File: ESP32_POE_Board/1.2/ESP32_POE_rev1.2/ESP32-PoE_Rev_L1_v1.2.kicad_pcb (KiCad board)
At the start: 4 copper layers, 81.5 x 92.3 mm, 133 parts, among them Q1 Q12MHz/20pF/10ppm/4P/3.2x2.5mm, Q2 BC817-40(SOT23), Q3 BC817-40(SOT23), T1 LMUN2211LT1G(SOT-23), U1 CH340T(SSOP20W), U2 TPS2375D(SO-8), U3 BL4054B-42TPRN(SOT23-5), U4 LAN8710A-EZC(QFN32), U5 TX4138(ESOIC-8), U6 ESP32-WROVER-E, U7 SY8089AAAC(SOT23-5), U8 SN74LVC1G04DBVR(SOT23-5)

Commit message: fixing POE board symbols + circuit
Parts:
- removed BAT_SENS_E1: Opened, OLIMEX_Jumpers-FP:SJ_1_SMALLER
- removed C22: 47uF/6.3V/20%/X5R/C0805, OLIMEX_RLC-FP:C_0805_5MIL_DWS
- removed CHRG1: LED/YELLOW/0603, OLIMEX_LEDs-FP:LED_0603_KA
- removed EXT1, EXT2: NS(HN1x10), OLIMEX_Connectors-FP:HN1x10
- removed FET1, FET2: WPM2015-3/TR, OLIMEX_Transistors-FP:SOT23
- removed L2: 2.2uH/1.5A/DCR=72mR/20%/3.00x3.00x1.50mm/CD32(NR3015T2R2M), OLIMEX_RLC-FP:CD32
- removed L5: FB0805/600R/2A, OLIMEX_RLC-FP:L_0805_5MIL_DWS
- removed PWR1: LED/RED/0603, OLIMEX_LEDs-FP:LED_0603_KA
- removed R17, R22: 470k/R0402, OLIMEX_RLC-FP:R_0402_5MIL_DWS
- removed R29: 220k/R0402, OLIMEX_RLC-FP:R_0402_5MIL_DWS
- removed R30: 49.9k/1%/R0402, OLIMEX_RLC-FP:R_0402_5MIL_DWS
- removed R39, R6: 10k/R0402, OLIMEX_RLC-FP:R_0402_5MIL_DWS
- removed R40, R45: 10R/R0402, OLIMEX_RLC-FP:R_0402_5MIL_DWS
- removed R46: 220R/R0402, OLIMEX_RLC-FP:R_0402_5MIL_DWS
- removed R8: 2.2k/R0402, OLIMEX_RLC-FP:R_0402_5MIL_DWS
- removed R9: 100k/R0402, OLIMEX_RLC-FP:R_0402_5MIL_DWS
- removed RM3: RA1206_(4X0603)_4B8_2.2k, OLIMEX_RLC-FP:R_MATRIX_4
- added C29: 1uF, Capacitor_SMD:C_0201_0603Metric, F.Cu at (159.8, 125.9)
- added C30: 10uF, Capacitor_SMD:C_0603_1608Metric, F.Cu at (156.0, 141.0)
- added C31: 1uF, Capacitor_SMD:C_0201_0603Metric, F.Cu at (159.8, 127.6)
- added D10: BAT54C, Package_TO_SOT_SMD:SOT-23, F.Cu at (147.1, 131.5)
- added D11: 1N5819, Diode_THT:D_DO-41_SOD81_P10.16mm_Horizontal, F.Cu at (146.5, 127.1)
- added FB1: 600R-2A, Capacitor_SMD:C_0805_2012Metric, F.Cu at (151.8, 141.3)
- added J1: USB_C_Receptacle, Connector_USB:USB_C_Receptacle_Molex_105450-0101-L, F.Cu at (155.7, 134.2)
- added J2: SI-46020-F, SI-46020-F:BEL_SI-46020-F, F.Cu at (153.1, 156.2)
- added Q4: BC817, Package_TO_SOT_SMD:SOT-23, F.Cu at (147.1, 135.9)
- added Q5: BC817, Package_TO_SOT_SMD:SOT-23, F.Cu at (147.1, 140.4)
- added U9: LAN8710A-EZC, LAN8710A_EZC:QFN32_5X5MC_MCH, F.Cu at (146.5, 167.6)
- C1: value 22uF/6.3V/20%/X5R/C0603 -> 10uF; footprint OLIMEX_RLC-FP:C_0603_5MIL_DWS -> Capacitor_SMD:C_0603_1608Metric
- C19: value 1nF/50V/10%/X7R/C0402 -> 1nF; footprint OLIMEX_RLC-FP:C_0402_5MIL_DWS -> Capacitor_SMD:C_1206_3216Metric; moved to F.Cu
- C28: value 100nF/16V/10%/X7R/C0402 -> 10uF; footprint OLIMEX_RLC-FP:C_0402_5MIL_DWS -> Capacitor_SMD:C_0603_1608Metric
- C3: value 47uF/6.3V/20%/X5R/C0805 -> 100nF; footprint OLIMEX_RLC-FP:C_0805_5MIL_DWS -> Capacitor_SMD:C_0402_1005Metric; moved to F.Cu
- C6: value 22uF/6.3V/20%/X5R/C0603 -> 1uF; footprint OLIMEX_RLC-FP:C_0603_5MIL_DWS -> Capacitor_SMD:C_0201_0603Metric
- D1, D3: value 1N5822/SS34/SMA -> 1N5819; footprint OLIMEX_Diodes-FP:SMA-KA -> Diode_THT:D_DO-41_SOD81_P10.16mm_Horizontal
- R1: value 10k/R0402 -> 1k; footprint OLIMEX_RLC-FP:R_0402_5MIL_DWS -> Resistor_SMD:R_0402_1005Metric
- R4: value 47k/R0402 -> 1k; footprint OLIMEX_RLC-FP:R_0402_5MIL_DWS -> Resistor_SMD:R_0402_1005Metric
- R5: value 2.2k/R0402 -> 220; footprint OLIMEX_RLC-FP:R_0402_5MIL_DWS -> Resistor_SMD:R_0402_1005Metric
- U3: value BL4054B-42TPRN(SOT23-5) -> FT232RQ; footprint OLIMEX_IC-FP:SOT-23-5 -> FT232RQ:QFN50P500X500X90-33N
- U7: value SY8089AAAC(SOT23-5) -> ESDS314DBVR; footprint OLIMEX_Regulators-FP:SOT-23-5 -> ESDS314DBVR:DBV0005A_N
- U8: value SN74LVC1G04DBVR(SOT23-5) -> MIC5504-3.3YM5; footprint OLIMEX_IC-FP:SOT-23-5 -> Package_TO_SOT_SMD:SOT-23-5
- moved C3 79.5 mm to (157.4, 169.4), turned to 0 degrees
- moved C19 62.0 mm to (153.1, 165.4)
- moved U7 58.3 mm to (158.6, 166.1), turned to 0 degrees
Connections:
- net /ESP_EN renamed ESP_EN
- net /GPIO2\HS2_DATA0 renamed GPIO2\HS2_DATA0
- C19 pad 1: Net-(BAT_SENS_E1-Pad2) -> GND
- C19 pad 2: GND -> Net-(C19-Pad2)
- C28 pad 1: GND -> +5VP
- C28 pad 2: +3.3VLAN -> GND
- C3 pad 1: Net-(MICRO_SD1-VDD) -> unconnected-(C3-Pad1)
- C3 pad 2: GND -> unconnected-(C3-Pad2)
- C6 pad 1: Net-(D3-K) -> +5V
- D1 pad 1: +5V -> Net-(D1-K)
- D1 pad 2: +5VP -> GPIO3_U0RXD
- D2 pad 2: /GPIO0 -> GPIO0
- D3 pad 1: Net-(D3-K) -> GPIO1_U0TXD
- D3 pad 2: +5V -> Net-(D3-A)
- R1 pad 1: +5V -> Net-(Q5-C)
- R1 pad 2: GND -> Net-(Q4-B)
- R4 pad 1: +5V -> Net-(Q4-E)
- R4 pad 2: /GPI39 -> Net-(Q5-B)
- R44 pad 1: /GPIO0 -> GPIO0
- R5 pad 2: GND -> Net-(D10-Pad3)
- U3 pad 1: Net-(U3-CHRGb) -> +5V
- U3 pad 2: GND -> Net-(D3-A)
- U3 pad 3: Net-(U3-VBAT) -> unconnected-(U3-~{RI}-Pad3)
- U3 pad 4: +5V -> Net-(U3-GND-Pad17)
- U3 pad 5: Net-(U3-PROG) -> (no net)
- U6 pad 25: /GPIO0 -> GPIO0
- U7 pad 1: Net-(D3-K) -> unconnected-(U7-I_O1-Pad1)
- U7 pad 2: GND -> unconnected-(U7-GND-Pad2)
- U7 pad 3: Net-(U7-LX) -> unconnected-(U7-I_O2-Pad3)
- U7 pad 4: Net-(D3-K) -> unconnected-(U7-I_O3-Pad4)
- U7 pad 5: Net-(U7-FB) -> unconnected-(U7-I_O4-Pad5)
- U8 pad 1: unconnected-(U8-NC-Pad1) -> +5VP
- U8 pad 2: /GPIO0 -> GND
- U8 pad 3: GND -> +5VP
- U8 pad 4: /GPIO17\EMAC_CLK_OUT_180 -> unconnected-(U8-NC-Pad4)
- U8 pad 5: +3.3VLAN -> +3.3V
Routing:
- net /GPIO0: track 67.8 -> 0.00 mm, vias 2 -> 0
- net /GPIO32: track 60.9 -> 0.00 mm, vias 2 -> 0
- net Net-(Q5-B): track 0.00 -> 60.8 mm, vias 0 -> 3
- net /GPI39: track 60.8 -> 0.00 mm, vias 3 -> 0
- net GND: track 380.7 -> 440.0 mm
- net GPIO0: track 0.00 -> 57.2 mm, vias 0 -> 2
- net (no net): track 0.00 -> 52.2 mm, vias 0 -> 3
- net Net-(D3-K): track 17.9 -> 0.00 mm
- net Net-(U7-FB): track 7.79 -> 0.00 mm, vias 2 -> 0
- net Net-(U3-CHRGb): track 5.24 -> 0.00 mm, vias 1 -> 0
- net Net-(U7-LX): track 4.89 -> 0.00 mm
- net Net-(BAT_SENS_E1-Pad2): track 2.97 -> 0.00 mm
- net +5V: track 91.6 -> 89.3 mm
- net Net-(Q5-C): track 0.00 -> 2.27 mm
- net Net-(U3-PROG): track 1.55 -> 0.00 mm
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
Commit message: updates
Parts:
- added SW1: PTS815 SJM 250 SMTR LFS, PTS815:SW4_PTS815 SJM 250 SMTR LFS_CNK, F.Cu at (179.0, 149.9)
- added SW2: PTS815 SJM 250 SMTR LFS, PTS815:SW4_PTS815 SJM 250 SMTR LFS_CNK, F.Cu at (179.0, 156.6)
- added U10: ESP32-WROOM-32, RF_Module:ESP32-WROOM-32, F.Cu at (198.3, 134.8)
- added U11: TPS2375D, LM193DR:D8, F.Cu at (186.8, 149.2)
- added U12: LM5145RGYR, LM5145RGYR:RGY0020B, F.Cu at (185.1, 155.5)

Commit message: fixing ethernet and poe power circuits
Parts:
- added C22: 22uF, Capacitor_SMD:C_0603_1608Metric, F.Cu at (215.6, 148.8)
- added C32: 100nF, Capacitor_SMD:C_0402_1005Metric, F.Cu at (223.1, 143.9)
- added C33: 2.2uF, Capacitor_SMD:C_0402_1005Metric, F.Cu at (223.1, 145.9)
- added C34: 100nF, Capacitor_SMD:C_0402_1005Metric, F.Cu at (223.1, 147.9)
- added C35: 100nF, Capacitor_SMD:C_0402_1005Metric, F.Cu at (223.1, 149.9)
- added D12: LED, LED_SMD:LED_0603_1608Metric, F.Cu at (224.3, 138.3)
- added D13: LED, LED_SMD:LED_0603_1608Metric, F.Cu at (224.3, 140.9)
- added D14: SMAJ58A, Diode_SMD:D_SMA, F.Cu at (217.6, 145.2)
- added R17: 2.2k, Resistor_SMD:R_0402_1005Metric, F.Cu at (217.9, 138.0)
- added R22: 130k, Resistor_SMD:R_0402_1005Metric, F.Cu at (217.9, 140.0)
- added R29: 10k, Resistor_SMD:R_0402_1005Metric, F.Cu at (217.9, 142.0)
- added R30: 10k, Resistor_SMD:R_0402_1005Metric, F.Cu at (220.8, 138.0)
- added R39: 4.42k, Resistor_SMD:R_0402_1005Metric, F.Cu at (220.8, 140.0)
- added R40: 24.9k, Resistor_SMD:R_0402_1005Metric, F.Cu at (220.8, 142.0)
- added R6: 2.2k, Resistor_SMD:R_0402_1005Metric, F.Cu at (215.0, 138.0)
- added R8: 2.2k, Resistor_SMD:R_0402_1005Metric, F.Cu at (215.0, 140.0)
- added R9: 2.2k, Resistor_SMD:R_0402_1005Metric, F.Cu at (215.0, 142.0)
- U12: value LM5145RGYR -> TX4138; footprint LM5145RGYR:RGY0020B -> TX4138:ESOIC8_XDS
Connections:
- C1 pad 1: +5V -> RCT
- C3 pad 1: unconnected-(C3-Pad1) -> GND
- C3 pad 2: unconnected-(C3-Pad2) -> RCT
- C6 pad 1: +5V -> RCT
- FB1 pad 1: +5V -> RCT
- J1 pad A1: +5V -> RCT
- J1 pad A12: +5V -> RCT
- J1 pad A4: +5V -> RCT
- J1 pad A9: +5V -> RCT
- J1 pad B1: +5V -> RCT
- J1 pad B12: +5V -> RCT
- J1 pad B4: +5V -> RCT
- J1 pad B9: +5V -> RCT
- J1 pad S1: +5V -> RCT
- J2 pad 1: unconnected-(J2-TD+-Pad1) -> TD+
- J2 pad 2: unconnected-(J2-TCT-Pad2) -> RCT
- J2 pad 3: unconnected-(J2-TD--Pad3) -> TD-
- J2 pad 4: unconnected-(J2-RD+-Pad4) -> RD+
- J2 pad 5: unconnected-(J2-RCT-Pad5) -> RCT
- J2 pad 6: unconnected-(J2-RD--Pad6) -> RD-
- LAN_CON1 pad 1: /TD+ -> TD+
- LAN_CON1 pad 2: /TD- -> TD-
- LAN_CON1 pad 3: /RD+ -> RD+
- LAN_CON1 pad 6: /RD- -> RD-
- R10 pad 2: /RD- -> RD-
- R11 pad 2: /RD+ -> RD+
- R12 pad 2: /TD- -> TD-
- R13 pad 2: /TD+ -> TD+
- TVS1 pad 1: /RD+ -> RD+
- TVS1 pad 3: /TD+ -> TD+
- TVS1 pad 4: /TD- -> TD-
- TVS1 pad 5: /RD- -> RD-
- TVS2 pad 1: /TD- -> TD-
- TVS2 pad 2: /TD+ -> TD+
- TVS3 pad 1: /RD+ -> RD+
- TVS3 pad 2: /RD- -> RD-
- U11 pad 1: unconnected-(U11-ILIM-Pad1) -> Net-(U11-ILIM)
- U11 pad 2: unconnected-(U11-CLASS-Pad2) -> Net-(U11-CLASS)
- U11 pad 3: unconnected-(U11-DET-Pad3) -> Net-(U11-DET)
- U11 pad 4: unconnected-(U11-VSS-Pad4) -> PW-
- U11 pad 5: unconnected-(U11-RTN-Pad5) -> GND
- U11 pad 7: unconnected-(U11-NC-Pad7) -> Net-(U11-NC)
- U3 pad 1: +5V -> RCT
- U3 pad 19: +5V -> RCT
- U4 pad 28: /TD- -> TD-
- U4 pad 29: /TD+ -> TD+
- U4 pad 30: /RD- -> RD-
- U4 pad 31: /RD+ -> RD+
- U7 pad 1: unconnected-(U7-I_O1-Pad1) -> TD+
- U7 pad 2: unconnected-(U7-GND-Pad2) -> GND
- U7 pad 3: unconnected-(U7-I_O2-Pad3) -> RD+
- U7 pad 4: unconnected-(U7-I_O3-Pad4) -> TD-
- U7 pad 5: unconnected-(U7-I_O4-Pad5) -> RD-
- U9 pad 1: unconnected-(U9-VDD2A-Pad1) -> RCT
- U9 pad 12: unconnected-(U9-VDDIO-Pad12) -> RCT
- U9 pad 15: unconnected-(U9-COL/CRS_DV/*MODE2-Pad15) -> GPIO27/EMAC_RX_CRS_DV
- U9 pad 16: unconnected-(U9-MDIO-Pad16) -> GPIO18/MDIO(RMII)
- U9 pad 2: unconnected-(U9-LED2/*NINTSEL-Pad2) -> Net-(D12-K)
- U9 pad 27: unconnected-(U9-VDD1A-Pad27) -> RCT
- U9 pad 3: unconnected-(U9-LED1/*REGOFF-Pad3) -> Net-(D13-A)
- U9 pad 5: unconnected-(U9-XTAL1/CLKIN-Pad5) -> GPIO17/EMAC_CLK_OUT_180
- U9 pad 6: unconnected-(U9-VDDCR-Pad6) -> RCT
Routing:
- net (no net): track 52.2 -> 141.6 mm
- net +5V: track 89.3 -> 0.00 mm, vias 4 -> 0
- net TD+: track 0.00 -> 25.5 mm, vias 0 -> 2
- net /TD+: track 25.5 -> 0.00 mm, vias 2 -> 0
- net /TD-: track 25.0 -> 0.00 mm, vias 2 -> 0
- net TD-: track 0.00 -> 24.9 mm, vias 0 -> 2
- net RD+: track 0.00 -> 13.3 mm, vias 0 -> 1
- net /RD+: track 13.3 -> 0.00 mm, vias 1 -> 0
- net RD-: track 0.00 -> 12.8 mm, vias 0 -> 1
- net /RD-: track 12.8 -> 0.00 mm, vias 1 -> 0
- net RCT: vias 0 -> 4

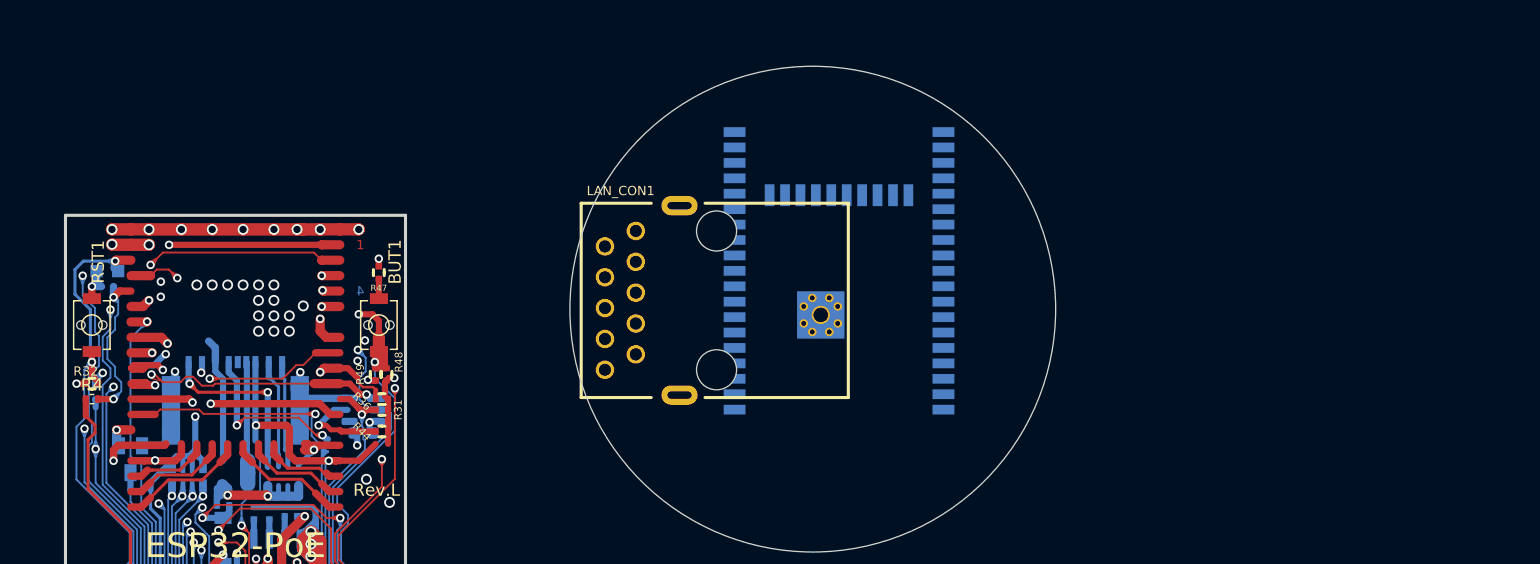
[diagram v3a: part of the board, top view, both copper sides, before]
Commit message: POE board partitioning
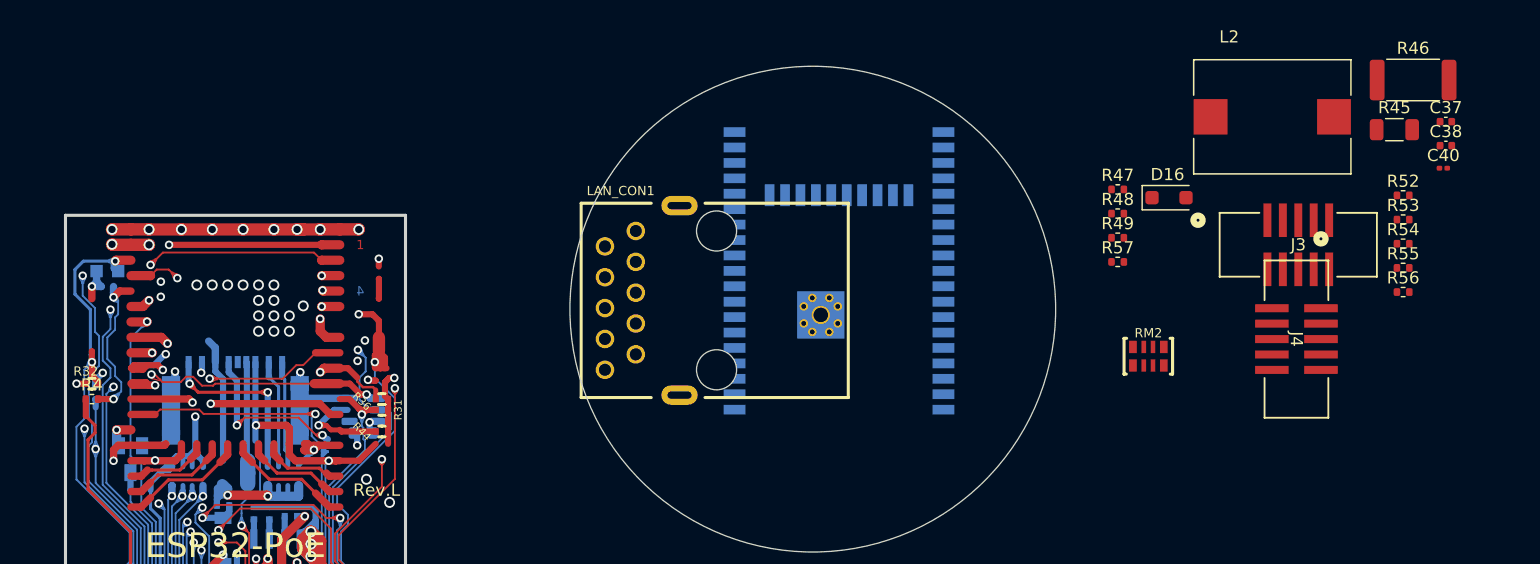
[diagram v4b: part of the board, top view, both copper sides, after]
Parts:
- removed BUT1, RST1: IT1185AU2, OLIMEX_Buttons-FP:IT1185AU2_V2
- added C37: 100nF, Capacitor_SMD:C_0402_1005Metric, F.Cu at (203.8, 82.4)
- added C38: 12pF, Capacitor_SMD:C_0402_1005Metric, F.Cu at (203.8, 84.4)
- added C40: 1uF, Capacitor_SMD:C_0201_0603Metric, F.Cu at (203.6, 86.3)
- added D16: PMEG6010CEH, Diode_SMD:D_SOD-123F, F.Cu at (181.0, 88.7)
- added J3: 3221-10-0300-00, 3221-10-0300-00:CONN10_3221-10-0300-00_CNC, F.Cu at (191.7, 92.6)
- added J4: Conn_02x05_Odd_Even, 3221-10-0300-00:CONN10_3221-10-0300-00_CNC, F.Cu at (191.5, 100.3)
- added L2: ASPI-0804T-330M-T, ASPI-0804T-330M-T:IND_ASPI-0804T-330M-T, F.Cu at (189.5, 82.0)
- added R45: 24.9k, Resistor_SMD:R_1206_3216Metric, F.Cu at (199.6, 83.1)
- added R46: 4.7k, Resistor_SMD:R_2512_6332Metric, F.Cu at (201.1, 79.0)
- added R52: 4.7, Resistor_SMD:R_0402_1005Metric, F.Cu at (200.3, 88.5)
- added R53: 30.1k, Resistor_SMD:R_0402_1005Metric, F.Cu at (200.3, 90.5)
- added R54: 5.23k, Resistor_SMD:R_0402_1005Metric, F.Cu at (200.3, 92.5)
- added R55: 10k, Resistor_SMD:R_0402_1005Metric, F.Cu at (200.3, 94.5)
- added R56: 10k, Resistor_SMD:R_0402_1005Metric, F.Cu at (200.3, 96.5)
- added R57: 2.2k, Resistor_SMD:R_0402_1005Metric, F.Cu at (176.8, 94.0)
- R47: value 220R/R0402 -> 10k; footprint OLIMEX_RLC-FP:R_0402_5MIL_DWS -> Resistor_SMD:R_0402_1005Metric
- R48: value 10k/R0402 -> 10k; footprint OLIMEX_RLC-FP:R_0402_5MIL_DWS -> Resistor_SMD:R_0402_1005Metric
- R49: value NA/R0402 -> 2.2k; footprint OLIMEX_RLC-FP:R_0402_5MIL_DWS -> Resistor_SMD:R_0402_1005Metric
- RM2: moved to F.Cu
- moved RM2 79.7 mm to (179.3, 101.8), turned to 180 degrees
- moved R49 62.1 mm to (176.8, 92.0), turned to 0 degrees
- moved R48 61.7 mm to (176.8, 90.0), turned to 0 degrees
- moved R47 61.2 mm to (176.8, 88.0), turned to 0 degrees
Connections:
- D4 pad 2: /GPI36\U1RXD -> GPI36\U1RXD
- D6 pad 2: /GPIO3\U0RXD -> GPIO3\U0RXD
- D7 pad 1: /GPIO1\U0TXD -> GPIO1\U0TXD
- R16 pad 1: /GPIO3\U0RXD -> GPIO3\U0RXD
- R19 pad 2: /GPIO3\U0RXD -> GPIO3\U0RXD
- R31 pad 2: /GPIO16\I2C-SCL -> GPIO16\I2C-SCL
- R35 pad 2: /GPIO13\I2C-SDA -> GPIO13\I2C-SDA
- R36 pad 2: /GPIO5\SPI_CS -> GPIO5\SPI_CS
- R37 pad 2: /GPI36\U1RXD -> GPI36\U1RXD
- R47 pad 1: Net-(BUT1-Pad2) -> unconnected-(R47-Pad1)
- R47 pad 2: GND -> unconnected-(R47-Pad2)
- R48 pad 1: +3.3V -> unconnected-(R48-Pad1)
- R48 pad 2: /GPI34\BUT1 -> unconnected-(R48-Pad2)
- R49 pad 1: /GPI34\BUT1 -> unconnected-(R49-Pad1)
- R49 pad 2: /D_Com -> unconnected-(R49-Pad2)
- RM2 pad 1.2: /GPIO26\EMAC_RXD1(RMII) -> GPIO26\EMAC_RXD1(RMII)
- RM2 pad 2.2: /GPIO25\EMAC_RXD0(RMII) -> GPIO25\EMAC_RXD0(RMII)
- RM2 pad 3.2: /GPIO27\EMAC_RX_CRS_DV -> GPIO27\EMAC_RX_CRS_DV
- RM2 pad 4.2: /GPIO18\MDIO(RMII) -> GPIO18\MDIO(RMII)
- SW1 pad 1: unconnected-(SW1-Pad1) -> GPI34\BUT1
- SW1 pad 2: unconnected-(SW1-Pad2) -> Net-(R56-Pad1)
- SW1 pad 4: unconnected-(SW1-Pad4) -> GND
- SW2 pad 1: unconnected-(SW2-Pad1) -> ESP_EN
- SW2 pad 4: unconnected-(SW2-Pad4) -> GND
- T1 pad 1: /GPIO12\PHY_PWR -> GPIO12\PHY_PWR
- U10 pad 1: Net-(U10-GND-Pad1) -> GND
- U10 pad 10: unconnected-(U10-IO25-Pad10) -> GPIO25\EMAC_RXD0(RMII)
- U10 pad 11: unconnected-(U10-IO26-Pad11) -> GPIO26\EMAC_RXD1(RMII)
- U10 pad 12: unconnected-(U10-IO27-Pad12) -> GPIO27\EMAC_RX_CRS_DV
- U10 pad 13: unconnected-(U10-IO14-Pad13) -> GPIO14\HS2_CLK
- U10 pad 14: unconnected-(U10-IO12-Pad14) -> GPIO12\PHY_PWR
- U10 pad 15: Net-(U10-GND-Pad1) -> GND
- U10 pad 16: unconnected-(U10-IO13-Pad16) -> GPIO13\I2C-SDA
- U10 pad 2: unconnected-(U10-VDD-Pad2) -> +3.3V
- U10 pad 23: unconnected-(U10-IO15-Pad23) -> GPIO15\HS2_CMD
- U10 pad 24: unconnected-(U10-IO2-Pad24) -> GPIO2\HS2_DATA0
- U10 pad 25: unconnected-(U10-IO0-Pad25) -> GPIO0
- U10 pad 26: unconnected-(U10-IO4-Pad26) -> GPIO4\U1TXD
- U10 pad 27: unconnected-(U10-IO16-Pad27) -> GPIO16\I2C-SCL
- U10 pad 28: unconnected-(U10-IO17-Pad28) -> GPIO17\EMAC_CLK_OUT_180
- U10 pad 29: unconnected-(U10-IO5-Pad29) -> GPIO5\SPI_CS
- U10 pad 3: unconnected-(U10-EN-Pad3) -> ESP_EN
- U10 pad 30: unconnected-(U10-IO18-Pad30) -> GPIO18\MDIO(RMII)
- U10 pad 31: unconnected-(U10-IO19-Pad31) -> GPIO19\EMAC_TXD0(RMII)
- U10 pad 33: unconnected-(U10-IO21-Pad33) -> GPIO21\EMAC_TX_EN(RMII)
- U10 pad 34: unconnected-(U10-RXD0/IO3-Pad34) -> GPIO3\U0RXD
- U10 pad 35: unconnected-(U10-TXD0/IO1-Pad35) -> GPIO1\U0TXD
- U10 pad 36: unconnected-(U10-IO22-Pad36) -> GPIO22\EMAC_TXD1(RMII)
- U10 pad 37: unconnected-(U10-IO23-Pad37) -> GPIO23\MDC(RMII)
- U10 pad 38: Net-(U10-GND-Pad1) -> GND
- U10 pad 39: Net-(U10-GND-Pad1) -> GND
- U10 pad 4: unconnected-(U10-SENSOR_VP-Pad4) -> GPI36\U1RXD
- U10 pad 5: unconnected-(U10-SENSOR_VN-Pad5) -> GPI39
- U10 pad 6: unconnected-(U10-IO34-Pad6) -> GPI34\BUT1
- U10 pad 7: unconnected-(U10-IO35-Pad7) -> GPI35
- U10 pad 8: unconnected-(U10-IO32-Pad8) -> GPIO32
- U10 pad 9: unconnected-(U10-IO33-Pad9) -> GPIO33
- U11 pad 6: unconnected-(U11-PG-Pad6) -> Net-(U11-PG)
- U11 pad 8: unconnected-(U11-VDD-Pad8) -> Net-(U11-DET)
- U12 pad 1: unconnected-(U12-SW-Pad1) -> Net-(D15-K)
- U12 pad 2: unconnected-(U12-ILIM-Pad2) -> Net-(R45-Pad2)
- U12 pad 3: unconnected-(U12-VIN-Pad3) -> Net-(U11-DET)
- U12 pad 4: unconnected-(U12-GND-Pad4) -> GND
- U12 pad 5: unconnected-(U12-FB-Pad5) -> Net-(U12-FB)
- U12 pad 6: unconnected-(U12-EN-Pad6) -> Net-(U11-PG)
- U12 pad 8: unconnected-(U12-BS-Pad8) -> Net-(U12-BS)
- U12 pad EPAD: unconnected-(U12-ILIM-PadEPAD) -> Net-(R45-Pad2)
- U4 pad 10: /GPIO26\EMAC_RXD1(RMII) -> GPIO26\EMAC_RXD1(RMII)
- U4 pad 11: /GPIO25\EMAC_RXD0(RMII) -> GPIO25\EMAC_RXD0(RMII)
- U4 pad 15: /GPIO27\EMAC_RX_CRS_DV -> GPIO27\EMAC_RX_CRS_DV
- U4 pad 16: /GPIO18\MDIO(RMII) -> GPIO18\MDIO(RMII)
- U4 pad 17: /GPIO23\MDC(RMII) -> GPIO23\MDC(RMII)
- U4 pad 21: /GPIO21\EMAC_TX_EN(RMII) -> GPIO21\EMAC_TX_EN(RMII)
- U4 pad 22: /GPIO19\EMAC_TXD0(RMII) -> GPIO19\EMAC_TXD0(RMII)
- U4 pad 23: /GPIO22\EMAC_TXD1(RMII) -> GPIO22\EMAC_TXD1(RMII)
- U4 pad 5: /GPIO17\EMAC_CLK_OUT_180 -> GPIO17\EMAC_CLK_OUT_180
- U6 pad 10: /GPIO25\EMAC_RXD0(RMII) -> GPIO25\EMAC_RXD0(RMII)
- U6 pad 11: /GPIO26\EMAC_RXD1(RMII) -> GPIO26\EMAC_RXD1(RMII)
- U6 pad 12: /GPIO27\EMAC_RX_CRS_DV -> GPIO27\EMAC_RX_CRS_DV
- U6 pad 13: /GPIO14\HS2_CLK -> GPIO14\HS2_CLK
- U6 pad 14: /GPIO12\PHY_PWR -> GPIO12\PHY_PWR
- U6 pad 16: /GPIO13\I2C-SDA -> GPIO13\I2C-SDA
- U6 pad 23: /GPIO15\HS2_CMD -> GPIO15\HS2_CMD
- U6 pad 26: /GPIO4\U1TXD -> GPIO4\U1TXD
- U6 pad 27: /GPIO16\I2C-SCL -> GPIO16\I2C-SCL
- U6 pad 28: /GPIO17\EMAC_CLK_OUT_180 -> GPIO17\EMAC_CLK_OUT_180
- U6 pad 29: /GPIO5\SPI_CS -> GPIO5\SPI_CS
- U6 pad 30: /GPIO18\MDIO(RMII) -> GPIO18\MDIO(RMII)
- U6 pad 31: /GPIO19\EMAC_TXD0(RMII) -> GPIO19\EMAC_TXD0(RMII)
- U6 pad 33: /GPIO21\EMAC_TX_EN(RMII) -> GPIO21\EMAC_TX_EN(RMII)
- U6 pad 34: /GPIO3\U0RXD -> GPIO3\U0RXD
- U6 pad 35: /GPIO1\U0TXD -> GPIO1\U0TXD
- U6 pad 36: /GPIO22\EMAC_TXD1(RMII) -> GPIO22\EMAC_TXD1(RMII)
- U6 pad 37: /GPIO23\MDC(RMII) -> GPIO23\MDC(RMII)
- U6 pad 4: /GPI36\U1RXD -> GPI36\U1RXD
- U6 pad 5: /GPI39 -> GPI39
- U6 pad 6: /GPI34\BUT1 -> GPI34\BUT1
- U6 pad 7: /GPI35 -> GPI35
- U6 pad 8: /GPIO32 -> GPIO32
- U6 pad 9: /GPIO33 -> GPIO33
- UEXT1 pad 10: /GPIO5\SPI_CS -> GPIO5\SPI_CS
- UEXT1 pad 3: /GPIO4\U1TXD -> GPIO4\U1TXD
- UEXT1 pad 5: /GPIO16\I2C-SCL -> GPIO16\I2C-SCL
- UEXT1 pad 6: /GPIO13\I2C-SDA -> GPIO13\I2C-SDA
- UEXT1 pad 7: /GPIO15\HS2_CMD -> GPIO15\HS2_CMD
- UEXT1 pad 9: /GPIO14\HS2_CLK -> GPIO14\HS2_CLK
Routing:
- net (no net): track 141.6 -> 314.0 mm
- net /GPI35: track 139.7 -> 0.00 mm, vias 5 -> 0
- net /GPIO1\U0TXD: track 99.3 -> 0.00 mm, vias 3 -> 0
- net GPIO16\I2C-SCL: track 0.00 -> 95.9 mm, vias 0 -> 4
- net /GPIO16\I2C-SCL: track 95.9 -> 0.00 mm, vias 4 -> 0
- net GPIO3\U0RXD: track 0.00 -> 95.6 mm, vias 0 -> 4
- net /GPIO3\U0RXD: track 95.6 -> 0.00 mm, vias 4 -> 0
- net GPIO14\HS2_CLK: track 0.00 -> 84.1 mm, vias 0 -> 2
- net /GPIO14\HS2_CLK: track 84.1 -> 0.00 mm, vias 2 -> 0
- net GPIO22\EMAC_TXD1(RMII): track 0.00 -> 84.1 mm, vias 0 -> 2
- net /GPIO22\EMAC_TXD1(RMII): track 84.1 -> 0.00 mm, vias 2 -> 0
- net GPIO19\EMAC_TXD0(RMII): track 0.00 -> 83.9 mm, vias 0 -> 3
- net /GPIO19\EMAC_TXD0(RMII): track 83.9 -> 0.00 mm, vias 3 -> 0
- net GPIO21\EMAC_TX_EN(RMII): track 0.00 -> 82.2 mm, vias 0 -> 3
- net /GPIO21\EMAC_TX_EN(RMII): track 82.2 -> 0.00 mm, vias 3 -> 0
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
